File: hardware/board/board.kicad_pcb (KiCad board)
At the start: 2 copper layers, 100 x 30 mm, 41 parts, among them J1 DC THRU, J2 DC THRU, J3 DC OUT, J4 DC IN, J5 DC IN, J6 DC OUT, J7 Eurorack Power, J8 Eurorack Power, SW1 ON/OFF, U1 VX7805-500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

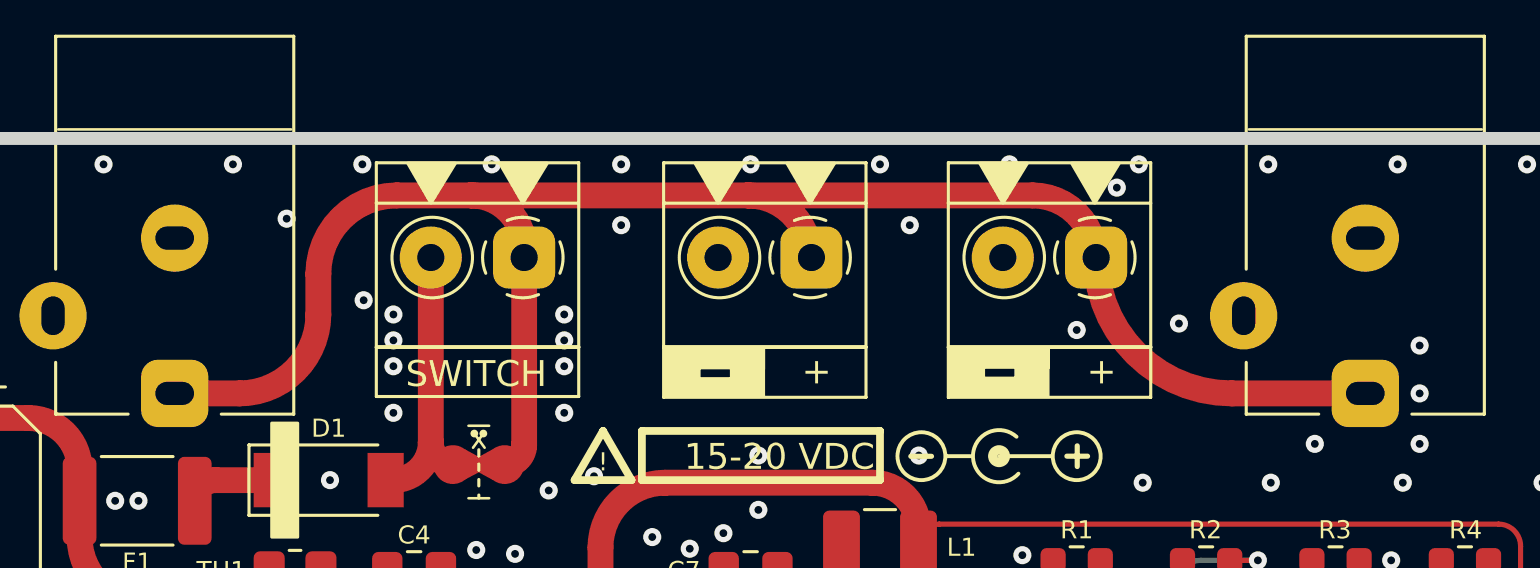
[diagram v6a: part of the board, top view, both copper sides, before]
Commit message: Widen some traces
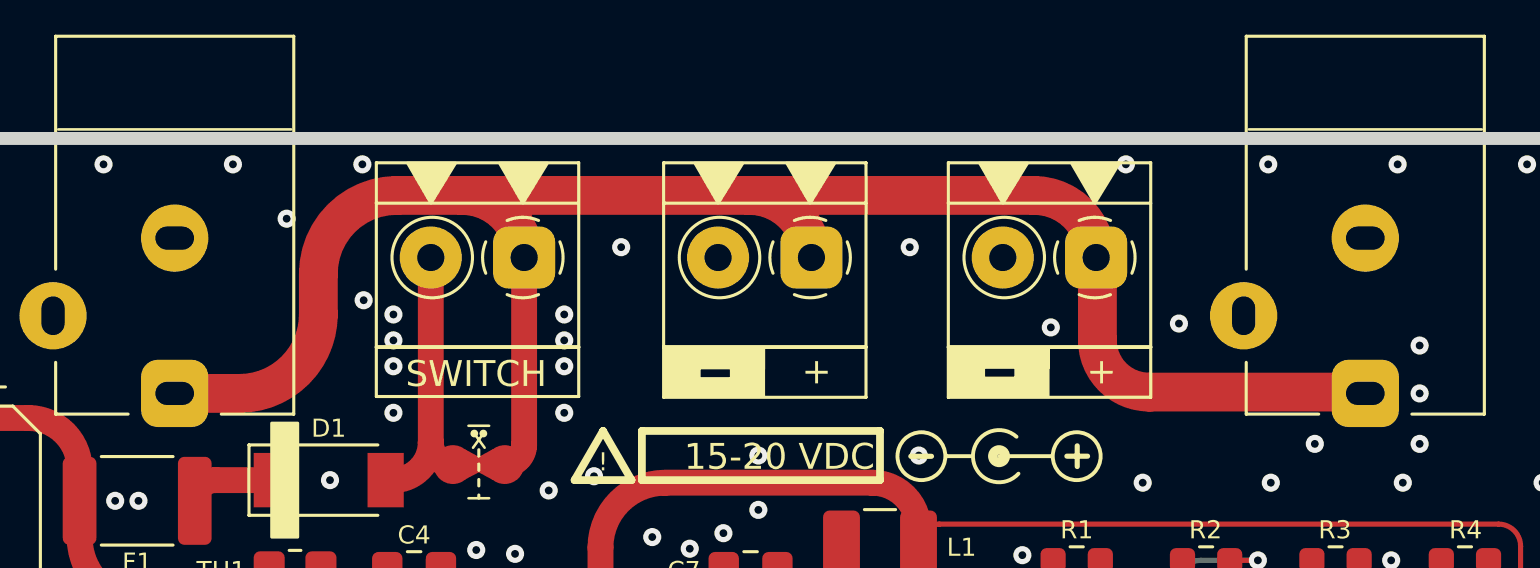
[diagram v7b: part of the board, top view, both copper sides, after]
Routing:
- net +VDC: track 70.4 -> 78.1 mm
- net GND: vias 173 -> 167
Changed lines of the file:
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@@
     )
     (pad_to_mask_clearance 0.0508)
+    (aux_axis_origin 58.5 93.075)
     (grid_origin 58.5 93.075)
     (pcbplotparams
@@
   (via (at 113.15 116.075) (size 0.7) (drill 0.3) (layers "F.Cu" "B.Cu") (free) (net 1))
   (via (at 115.6 113.675) (size 0.7) (drill 0.3) (layers "F.Cu" "B.Cu") (free) (net 1))
-  (via (at 90.5 96.425) (size 0.7) (drill 0.3) (layers "F.Cu" "B.Cu") (free) (net 1))
+  (via (at 90.5 97.275) (size 0.7) (drill 0.3) (layers "F.Cu" "B.Cu") (free) (net 1))
   (via (at 148.3 105.375) (size 0.7) (drill 0.3) (layers "F.Cu" "B.Cu") (free) (net 1))
   (via (at 61.7 107.325) (size 0.7) (drill 0.3) (layers "F.Cu" "B.Cu") (free) (net 1))
@@
   (via (at 117.3 104.875) (size 0.7) (drill 0.3) (layers "F.Cu" "B.Cu") (free) (net 1))
   (via (at 138.5 119.075) (size 0.7) (drill 0.3) (layers "F.Cu" "B.Cu") (free) (net 1))
-  (via (at 110.5 94.075) (size 0.7) (drill 0.3) (layers "F.Cu" "B.Cu") (free) (net 1))
   (via (at 75.5 122.075) (size 0.7) (drill 0.3) (layers "F.Cu" "B.Cu") (free) (net 1))
   (via (at 145.5 94.075) (size 0.7) (drill 0.3) (layers "F.Cu" "B.Cu") (free) (net 1))
   (via (at 65.7 114.775) (size 0.7) (drill 0.3) (layers "F.Cu" "B.Cu") (free) (net 1))
   (via (at 132 119.075) (size 0.7) (drill 0.3) (layers "F.Cu" "B.Cu") (free) (net 1))
-  (via (at 100.5 94.075) (size 0.7) (drill 0.3) (layers "F.Cu" "B.Cu") (free) (net 1))
   (via (at 59.5 115.075) (size 0.7) (drill 0.3) (layers "F.Cu" "B.Cu") (free) (net 1))
   (via (at 150.5 122.075) (size 0.7) (drill 0.3) (layers "F.Cu" "B.Cu") (free) (net 1))
-  (via (at 85.5 94.075) (size 0.7) (drill 0.3) (layers "F.Cu" "B.Cu") (free) (net 1))
   (via (at 59.5 100.075) (size 0.7) (drill 0.3) (layers "F.Cu" "B.Cu") (free) (net 1))
   (via (at 65.5 122.075) (size 0.7) (drill 0.3) (layers "F.Cu" "B.Cu") (free) (net 1))
@@
   (via (at 145.5 122.075) (size 0.7) (drill 0.3) (layers "F.Cu" "B.Cu") (free) (net 1))
   (via (at 65.7 112.775) (size 0.7) (drill 0.3) (layers "F.Cu" "B.Cu") (free) (net 1))
-  (via (at 101.65 96.425) (size 0.7) (drill 0.3) (layers "F.Cu" "B.Cu") (free) (net 1))
-  (via (at 108.1 100.475) (size 0.7) (drill 0.3) (layers "F.Cu" "B.Cu") (free) (net 1))
+  (via (at 101.65 97.275) (size 0.7) (drill 0.3) (layers "F.Cu" "B.Cu") (free) (net 1))
+  (via (at 107.1 100.375) (size 0.7) (drill 0.3) (layers "F.Cu" "B.Cu") (free) (net 1))
   (via (at 79.25 106.275) (size 0.7) (drill 0.3) (layers "F.Cu" "B.Cu") (free) (net 1))
   (via (at 81.7 103.675) (size 0.7) (drill 0.3) (layers "F.Cu" "B.Cu") (free) (net 1))
@@
   (via (at 148.3 103.175) (size 0.7) (drill 0.3) (layers "F.Cu" "B.Cu") (free) (net 1))
   (via (at 139.5 102.875) (size 0.7) (drill 0.3) (layers "F.Cu" "B.Cu") (free) (net 1))
-  (via (at 90.5 94.075) (size 0.7) (drill 0.3) (layers "F.Cu" "B.Cu") (free) (net 1))
   (via (at 79.25 117.575) (size 0.7) (drill 0.3) (layers "F.Cu" "B.Cu") (free) (net 1))
   (via (at 113.15 113.675) (size 0.7) (drill 0.3) (layers "F.Cu" "B.Cu") (free) (net 1))
@@
   (via (at 95.5 122.075) (size 0.7) (drill 0.3) (layers "F.Cu" "B.Cu") (free) (net 1))
   (via (at 64.7 107.325) (size 0.7) (drill 0.3) (layers "F.Cu" "B.Cu") (free) (net 1))
-  (via (at 105.5 94.075) (size 0.7) (drill 0.3) (layers "F.Cu" "B.Cu") (free) (net 1))
   (via (at 120.5 94.075) (size 0.7) (drill 0.3) (layers "F.Cu" "B.Cu") (free) (net 1))
   (via (at 64.7 108.275) (size 0.7) (drill 0.3) (layers "F.Cu" "B.Cu") (free) (net 1))
   (via (at 65.7 109.275) (size 0.7) (drill 0.3) (layers "F.Cu" "B.Cu") (free) (net 1))
   (via (at 81.3 119.825) (size 0.7) (drill 0.3) (layers "F.Cu" "B.Cu") (free) (net 1))
-  (via (at 95.5 94.075) (size 0.7) (drill 0.3) (layers "F.Cu" "B.Cu") (free) (net 1))
   (via (at 157.5 106.075) (size 0.7) (drill 0.3) (layers "F.Cu" "B.Cu") (free) (net 1))
   (via (at 63.7 114.775) (size 0.7) (drill 0.3) (layers "F.Cu" "B.Cu") (free) (net 1))
@@
   (via (at 70.5 94.075) (size 0.7) (drill 0.3) (layers "F.Cu" "B.Cu") (free) (net 1))
   (via (at 130.5 122.075) (size 0.7) (drill 0.3) (layers "F.Cu" "B.Cu") (free) (net 1))
+  (via (at 110 94.075) (size 0.7) (drill 0.3) (layers "F.Cu" "B.Cu") (free) (net 1))
   (via (at 81.7 99.875) (size 0.7) (drill 0.3) (layers "F.Cu" "B.Cu") (free) (net 1))
-  (via (at 109.65 94.975) (size 0.7) (drill 0.3) (layers "F.Cu" "B.Cu") (free) (net 1))
   (via (at 62.7 107.325) (size 0.7) (drill 0.3) (layers "F.Cu" "B.Cu") (free) (net 1))
   (via (at 88.3 100.875) (size 0.7) (drill 0.3) (layers "F.Cu" "B.Cu") (free) (net 1))
@@
   (arc (start 100.54 115.04) (mid 100.257358 114.357642) (end 99.575 114.075) (width 1) (layer "F.Cu") (net 7))
   (segment (start 107.00455 111.382951) (end 109.0125 109.375) (width 0.2) (layer "F.Cu") (net 8))
-  (segment (start 78.8 98.3) (end 78.8 99.875) (width 1) (layer "F.Cu") (net 9))
-  (segment (start 95.4 95.275) (end 106.4 95.275) (width 1) (layer "F.Cu") (net 9))
+  (segment (start 84.7 95.275) (end 95.4508 95.275) (width 1.5) (layer "F.Cu") (net 9))
+  (segment (start 108.9 100.875) (end 108.9 97.7242) (width 1.5) (layer "F.Cu") (net 9))
+  (segment (start 95.4508 95.275) (end 106.4508 95.275) (width 1.5) (layer "F.Cu") (net 9))
   (segment (start 84.7 95.275) (end 81.825 95.275) (width 1) (layer "F.Cu") (net 9))
   (segment (start 86.7508 97.675) (end 86.7508 97.3258) (width 1) (layer "F.Cu") (net 9))
-  (segment (start 75.75 102.925) (end 73.25 102.925) (width 1) (layer "F.Cu") (net 9))
+  (segment (start 73.25 102.925) (end 75.75 102.925) (width 1.5) (layer "F.Cu") (net 9))
+  (segment (start 119.2 102.875) (end 110.9 102.875) (width 1.5) (layer "F.Cu") (net 9))
   (segment (start 86.7508 97.675) (end 86.7508 104.9242) (width 1) (layer "F.Cu") (net 9))
-  (segment (start 119.25 102.925) (end 114.1008 102.925) (width 1) (layer "F.Cu") (net 9))
-  (segment (start 95.4 95.275) (end 84.7 95.275) (width 1) (layer "F.Cu") (net 9))
+  (segment (start 78.8 99.875) (end 78.8 98.3) (width 1.5) (layer "F.Cu") (net 9))
+  (segment (start 81.825 95.275) (end 84.3508 95.275) (width 1.5) (layer "F.Cu") (net 9))
+  (arc (start 95.4508 95.275) (mid 97.147856 95.977944) (end 97.8508 97.675) (width 1.5) (layer "F.Cu") (net 9))
   (arc (start 86.7508 104.9242) (mid 86.530896 105.455096) (end 86 105.675) (width 1) (layer "F.Cu") (net 9))
-  (arc (start 95.4 95.275) (mid 97.097056 95.977944) (end 97.8 97.675) (width 1) (layer "F.Cu") (net 9))
+  (arc (start 84.3508 95.275) (mid 86.047856 95.977944) (end 86.7508 97.675) (width 1.5) (layer "F.Cu") (net 9))
+  (arc (start 119.25 102.925) (mid 119.235355 102.889645) (end 119.2 102.875) (width 1.5) (layer "F.Cu") (net 9))
   (arc (start 86.7508 97.3258) (mid 86.150135 95.875665) (end 84.7 95.275) (width 1) (layer "F.Cu") (net 9))
-  (arc (start 114.1008 102.925) (mid 110.388489 101.387311) (end 108.8508 97.675) (width 1) (layer "F.Cu") (net 9))
-  (arc (start 81.825 95.275) (mid 79.686002 96.161002) (end 78.8 98.3) (width 1) (layer "F.Cu") (net 9))
-  (arc (start 106.4 95.275) (mid 108.097056 95.977944) (end 108.8 97.675) (width 1) (layer "F.Cu") (net 9))
-  (arc (start 78.8 99.875) (mid 77.906676 102.031676) (end 75.75 102.925) (width 1) (layer "F.Cu") (net 9))
+  (arc (start 110.9 102.875) (mid 109.485786 102.289214) (end 108.9 100.875) (width 1.5) (layer "F.Cu") (net 9))
+  (arc (start 75.75 102.925) (mid 77.906676 102.031676) (end 78.8 99.875) (width 1.5) (layer "F.Cu") (net 9))
+  (arc (start 78.8 98.3) (mid 79.686002 96.161002) (end 81.825 95.275) (width 1.5) (layer "F.Cu") (net 9))
+  (arc (start 106.4508 95.275) (mid 108.147856 95.977944) (end 108.8508 97.675) (width 1.5) (layer "F.Cu") (net 9))
+  (arc (start 108.9 97.7242) (mid 108.88559 97.68941) (end 108.8508 97.675) (width 1.5) (layer "F.Cu") (net 9))
   (segment (start 76.9 109.725) (end 76.9 109.975) (width 1) (layer "F.Cu") (net 10))
   (segment (start 100.2 106.375) (end 92.2 106.375) (width 1) (layer "F.Cu") (net 10))
